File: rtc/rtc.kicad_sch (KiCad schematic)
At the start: 9 parts, among them J1 Conn_01x04_Pin, U1 PCF8563T/5_518, Y1 Crystal

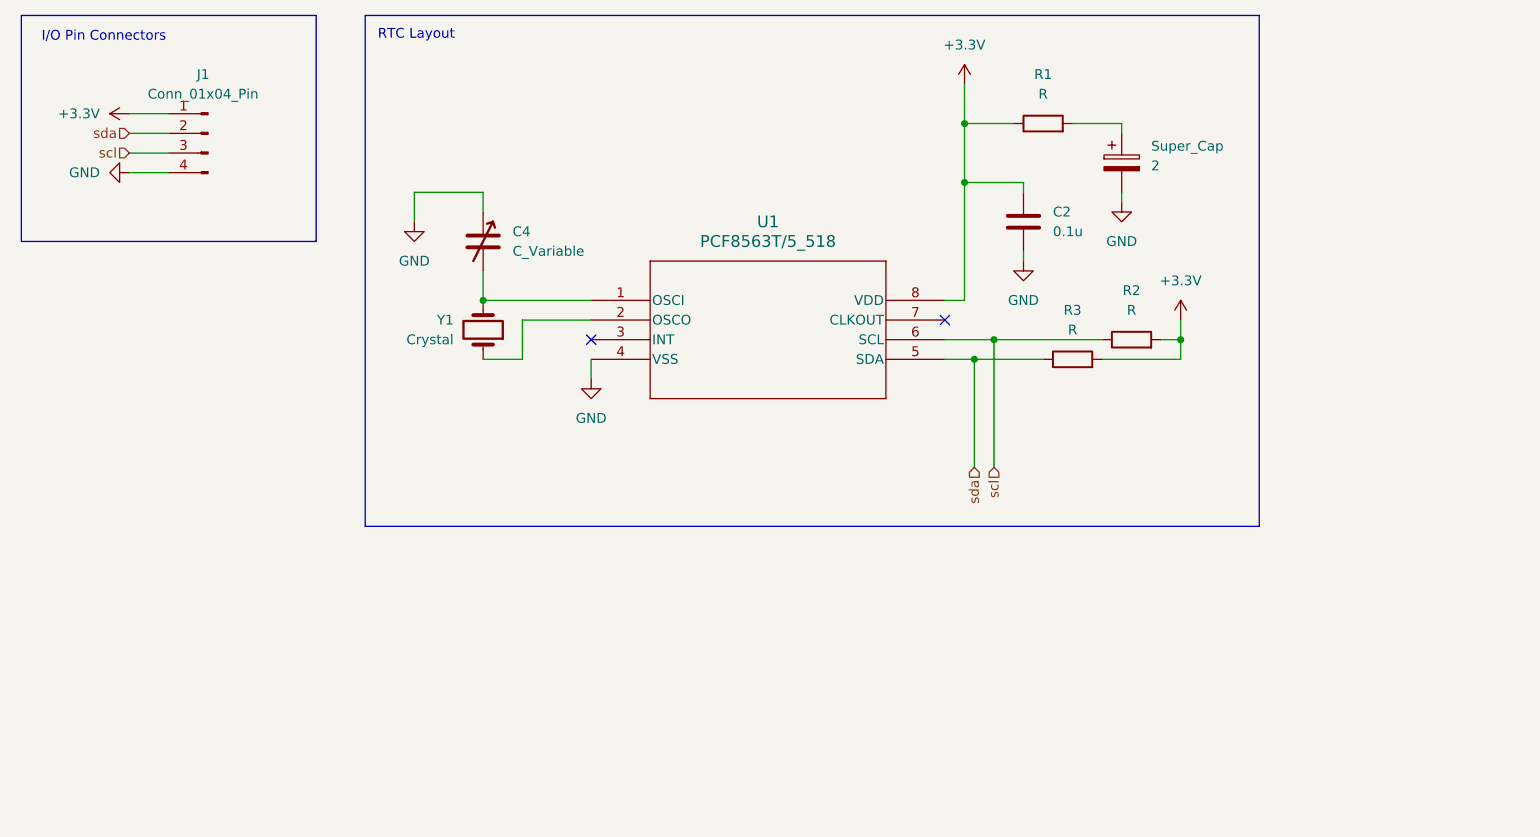
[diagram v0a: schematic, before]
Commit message: rtc schematic progress
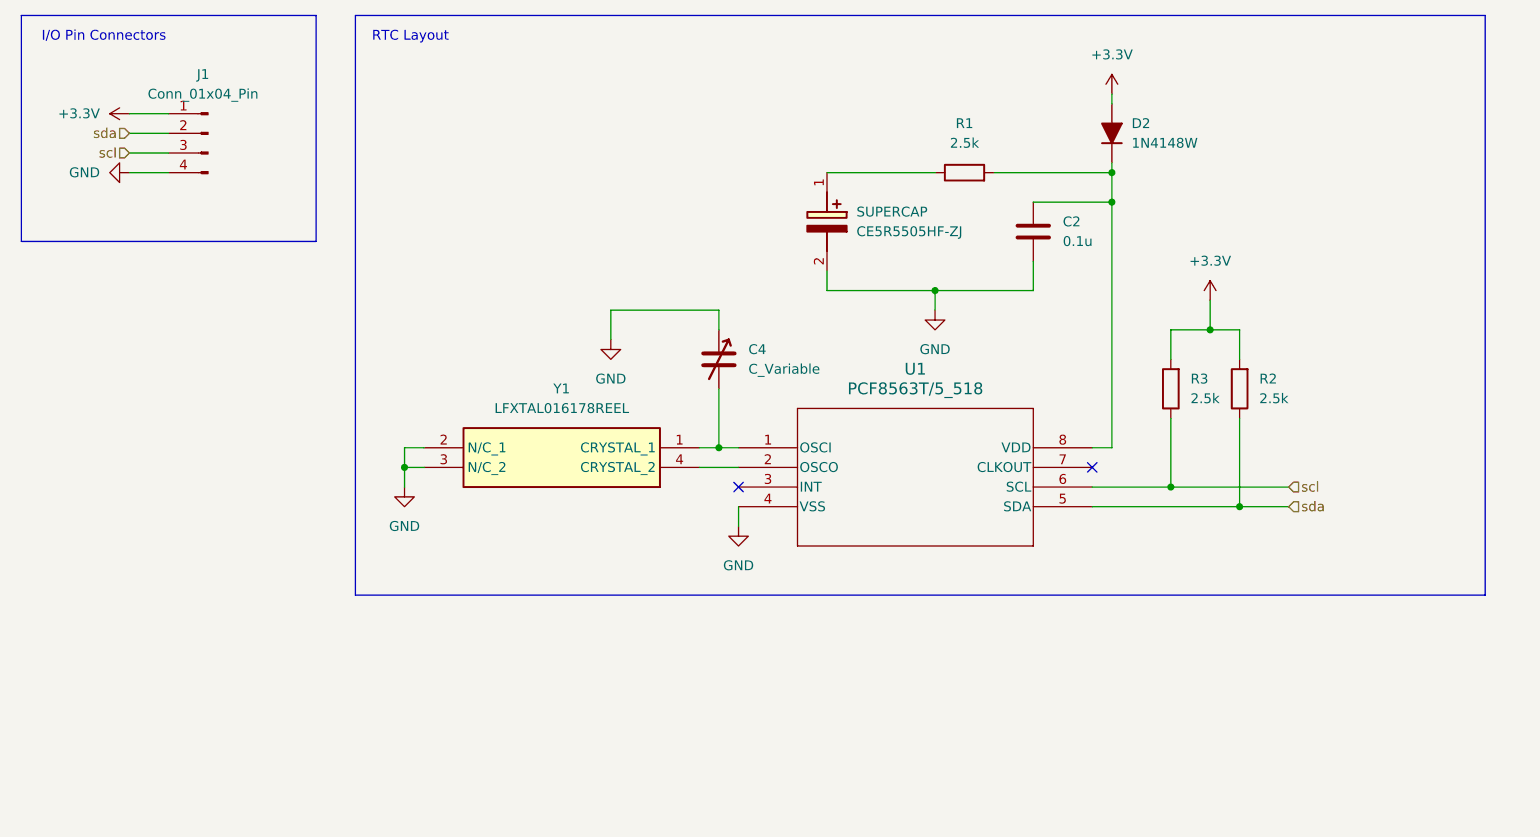
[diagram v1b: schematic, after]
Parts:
- removed Super_Cap: 2, symbol Device:C_Polarized
- removed Y1: Crystal, symbol Device:Crystal
- added D2: 1N4148W, PCM_Diode_SMD_AKL:D_SOD-123, symbol PCM_Diode_AKL:1N4148W
- added SUPERCAP: CE5R5505HF-ZJ, CE5R5505HFZJ, symbol CE5R5505HF-ZJ:CE5R5505HF-ZJ
- added Y1: LFXTAL016178REEL, LFXTAL016178REEL, symbol LFXTAL016178REEL:LFXTAL016178REEL
- R1, R2, R3: value R -> 2.5k
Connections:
- net +3.3V: now also D2.2 (A); no longer C2.1, R1.1, U1.8 (VDD)
- net GND: now also SUPERCAP.2 (-), Y1.2 (N/C_1), Y1.3 (N/C_2)
- net scl: now also R3.1; no longer R2.1
- net sda: now also R2.1; no longer R3.1
- net at C4.2, U1.1 (OSCI): now also Y1.1 (CRYSTAL_1)
- net at U1.2 (OSCO): now also Y1.4 (CRYSTAL_2)
- net at R1.2: now also C2.1, U1.8 (VDD), D2.1 (K)
- new net: R1.1, SUPERCAP.1 (+)
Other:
- moved on the sheet: C2, C4, R1, R2, R3, U1

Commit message: finished rtc schematic
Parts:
- removed C4: C_Variable, symbol Device:C_Variable
- added C1: C, Capacitor_SMD:C_0402_1005Metric_Pad0.74x0.62mm_HandSolder, symbol Device:C
- C2: footprint (none) -> Capacitor_SMD:C_0402_1005Metric_Pad0.74x0.62mm_HandSolder
- J1: footprint (none) -> Connector_PinHeader_2.54mm:PinHeader_1x04_P2.54mm_Horizontal
- R1: value 2.5k -> 20k; footprint (none) -> Resistor_SMD:R_0402_1005Metric_Pad0.72x0.64mm_HandSolder
- R2, R3: footprint (none) -> Resistor_SMD:R_0402_1005Metric_Pad0.72x0.64mm_HandSolder
- SUPERCAP1: renamed from SUPERCAP; value CE5R5505HF-ZJ -> 5; footprint CE5R5505HFZJ -> pcb_footprints:CE5R5505HFZJ
- U1: footprint U_SO8_NXP -> pcb_footprints:PCF8563T_5_518_U_SO8_NXP
- Y1: footprint LFXTAL016178REEL -> pcb_footprints:LFXTAL016178REEL
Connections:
- net GND: now also C1.1
- net at U1.1 (OSCI), Y1.1 (CRYSTAL_1): now also C1.2
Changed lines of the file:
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@@
 			)
 		)
-		(property "Footprint" "U_SO8_NXP"
+		(property "Footprint" "pcb_footprints:PCF8563T_5_518_U_SO8_NXP"
 			(at 125.73 86.36 0)
 			(effects
@@
 			)
 		)
-		(property "Footprint" "LFXTAL016178REEL"
+		(property "Footprint" "pcb_footprints:LFXTAL016178REEL"
 			(at 88.9 -6.02 0)
 			(effects
@@
 			)
 		)
-		(property "Footprint" ""
+		(property "Footprint" "Connector_PinHeader_2.54mm:PinHeader_1x04_P2.54mm_Horizontal"
 			(at 57.15 45.72 0)
 			(effects
@@
 			)
 		)
-		(property "Value" "2.5k"
+		(property "Value" "20k"
 			(at 154.94 46.99 90)
 			(effects
@@
 			)
 		)
-		(property "Footprint" ""
+		(property "Footprint" "Resistor_SMD:R_0402_1005Metric_Pad0.72x0.64mm_HandSolder"
 			(at 154.94 52.578 90)
 			(effects
@@
 			)
 		)
-		(property "Footprint" ""
+		(property "Footprint" "Capacitor_SMD:C_0402_1005Metric_Pad0.74x0.62mm_HandSolder"
 			(at 164.7952 62.23 0)
 			(effects
@@
 			)
 		)
-		(property "Footprint" ""
+		(property "Footprint" "Resistor_SMD:R_0402_1005Metric_Pad0.72x0.64mm_HandSolder"
 			(at 183.388 78.74 90)
 			(effects
@@
 		(dnp no)
 		(fields_autoplaced yes)
-		(property "Reference" "SUPERCAP"
+		(property "Reference" "SUPERCAP1"
 			(at 140.97 55.8799 90)
 			(effects
@@
 			)
 		)
-		(property "Value" "CE5R5505HF-ZJ"
+		(property "Value" "5"
 			(at 140.97 58.4199 90)
 			(effects
@@
 			)
 		)
-		(property "Footprint" "CE5R5505HFZJ"
+		(property "Footprint" "pcb_footprints:CE5R5505HFZJ"
 			(at 40.97 59.69 0)
 			(effects
@@
 			(project ""
 				(path "/818bb878-dad3-4efb-a0ef-59b01bf8b5c9"
-					(reference "SUPERCAP")
+					(reference "SUPERCAP1")
 					(unit 1)
 				)
@@
 			)
 		)
-		(property "Footprint" ""
+		(property "Footprint" "Resistor_SMD:R_0402_1005Metric_Pad0.72x0.64mm_HandSolder"
 			(at 192.278 78.74 90)
 			(effects
@@
 	)
 	(symbol
-		(lib_id "Device:C_Variable")
+		(lib_id "Device:C")
 		(at 123.19 74.93 0)
 		(unit 1)
@@
 		(dnp no)
 		(fields_autoplaced yes)
-		(property "Reference" "C4"
+		(property "Reference" "C1"
 			(at 127 73.6599 0)
 			(effects
@@
 			)
 		)
-		(property "Value" "C_Variable"
+		(property "Value" "C"
 			(at 127 76.1999 0)
 			(effects
@@
 			)
 		)
-		(property "Footprint" ""
-			(at 123.19 74.93 0)
+		(property "Footprint" "Capacitor_SMD:C_0402_1005Metric_Pad0.74x0.62mm_HandSolder"
+			(at 124.1552 78.74 0)
 			(effects
 				(font
@@
 			)
 		)
-		(property "Description" "Variable capacitor"
+		(property "Description" "Unpolarized capacitor"
 			(at 123.19 74.93 0)
 			(effects
@@
 			(project ""
 				(path "/818bb878-dad3-4efb-a0ef-59b01bf8b5c9"
-					(reference "C4")
-					(unit 1)
-				)
+					(reference "C1")
+					(unit 1)
+				)

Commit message: finished rtc schematic
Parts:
- removed D2: 1N4148W, PCM_Diode_SMD_AKL:D_SOD-123, symbol PCM_Diode_AKL:1N4148W
- removed J1: Conn_01x04_Pin, Connector_PinHeader_2.54mm:PinHeader_1x04_P2.54mm_Horizontal, symbol Connector:Conn_01x04_Pin
- added C3: C, Capacitor_SMD:C_0402_1005Metric_Pad0.74x0.62mm_HandSolder, symbol Device:C
- added D2: RB751V-40X_R1, pcb_footprints:SODFL2512X90N, symbol PCM_Diode_Schottky_AKL:D_Schottky_Generic
- added J1: Conn_02x03_Counter_Clockwise, Connector_PinHeader_2.54mm:PinHeader_2x03_P2.54mm_Vertical, symbol Connector_Generic:Conn_02x03_Counter_Clockwise
- added J2, J3, J4: Conn_01x04, pcb_footprints:JST_SH_BM04B-SRSS-TB_1x04-1MP_P1.00mm_Vertical, symbol Connector_Generic:Conn_01x04
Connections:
- net +3.3V: now also D2.2 (A), J1.1 (Pin_1), J2.2 (Pin_2), J3.2 (Pin_2), J4.2 (Pin_2)
- net GND: now also C1.2, C3.2, J1.4 (Pin_4), J2.1 (Pin_1), J3.1 (Pin_1), J4.1 (Pin_1); no longer C1.1
- net scl: now also J1.3 (Pin_3), J2.4 (Pin_4), J3.4 (Pin_4), J4.4 (Pin_4)
- net sda: now also J1.2 (Pin_2), J2.3 (Pin_3), J3.3 (Pin_3), J4.3 (Pin_3)
- net at U1.1 (OSCI), Y1.1 (CRYSTAL_1): now also C1.1; no longer C1.2
- net at U1.2 (OSCO), Y1.4 (CRYSTAL_2): now also C3.1
- net at C2.1, R1.2, U1.8 (VDD): now also D2.1 (K)
- no-connect marks 2 -> 4
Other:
- note added: "JST Connectors"
- moved on the sheet: C1, C2, R1, R2, R3, SUPERCAP1, U1, Y1

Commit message: finished rtc pcb
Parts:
- removed J1: Conn_02x03_Counter_Clockwise, Connector_PinHeader_2.54mm:PinHeader_2x03_P2.54mm_Vertical, symbol Connector_Generic:Conn_02x03_Counter_Clockwise
- added J1: Conn_02x03_Odd_Even, Connector_PinHeader_2.54mm:PinHeader_2x03_P2.54mm_Vertical, symbol Connector_Generic:Conn_02x03_Odd_Even
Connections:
- net +3.3V: now also J1.1 (Pin_1)
- net GND: now also J1.6 (Pin_6)
- net scl: now also J1.5 (Pin_5)
- net sda: now also J1.3 (Pin_3)
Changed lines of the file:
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@@
 	)
 	(no_connect
-		(at 180.34 87.63)
+		(at 60.96 46.99)
 	)
 	(no_connect
-		(at 60.96 46.99)
+		(at 180.34 87.63)
 	)
 	(no_connect
@@
 	(wire
 		(pts
-			(xy 43.18 46.99) (xy 48.26 46.99)
-		)
-		(stroke
-			(width 0)
-			(type default)
-		)
-	)
-	(wire
-		(pts
 			(xy 44.45 111.76) (xy 49.53 111.76)
 		)
@@
 	(wire
 		(pts
-			(xy 172.72 53.34) (xy 182.88 53.34)
+			(xy 43.18 49.53) (xy 48.26 49.53)
 		)
 		(stroke
@@
 	(wire
 		(pts
-			(xy 43.18 44.45) (xy 48.26 44.45)
+			(xy 172.72 53.34) (xy 182.88 53.34)
 		)
 		(stroke
@@
 	(wire
 		(pts
-			(xy 113.03 80.01) (xy 115.57 80.01)
+			(xy 43.18 44.45) (xy 48.26 44.45)
 		)
 		(stroke
@@
 	(wire
 		(pts
-			(xy 43.18 49.53) (xy 48.26 49.53)
+			(xy 113.03 80.01) (xy 115.57 80.01)
 		)
 		(stroke
@@
 		)
 	)
+	(wire
+		(pts
+			(xy 43.18 46.99) (xy 48.26 46.99)
+		)
+		(stroke
+			(width 0)
+			(type default)
+		)
+	)
 	(image
 		(at 52.07 66.04)
@@
 		)
 	)
-	(hierarchical_label "scl"
+	(global_label "scl"
 		(shape input)
-		(at 205.74 90.17 0)
+		(at 43.18 49.53 180)
+		(fields_autoplaced yes)
 		(effects
 			(font
 				(size 1.27 1.27)
 			)
-			(justify left)
+			(justify right)
+		)
+		(property "Intersheetrefs" "${INTERSHEET_REFS}"
+			(at 37.4129 49.53 0)
+			(effects
+				(font
+					(size 1.27 1.27)
+				)
+				(justify right)
+				(hide yes)
+			)
 		)
 	)
-	(hierarchical_label "sda"
+	(global_label "sda"
 		(shape input)
-		(at 44.45 111.76 180)
+		(at 205.74 92.71 0)
+		(fields_autoplaced yes)
 		(effects
 			(font
 				(size 1.27 1.27)
 			)
-			(justify right)
+			(justify left)
+		)
+		(property "Intersheetrefs" "${INTERSHEET_REFS}"
+			(at 212.0513 92.71 0)
+			(effects
+				(font
+					(size 1.27 1.27)
+				)
+				(justify left)
+				(hide yes)
+			)
 		)
 	)
-	(hierarchical_label "sda"
+	(global_label "sda"
 		(shape input)
-		(at 43.18 46.99 180)
+		(at 44.45 125.73 180)
+		(fields_autoplaced yes)
 		(effects
 			(font
@@
 			(justify right)
 		)
+		(property "Intersheetrefs" "${INTERSHEET_REFS}"
+			(at 38.1387 125.73 0)
+			(effects
+				(font
+					(size 1.27 1.27)
+				)
+				(justify right)
+				(hide yes)
+			)
+		)
 	)
-	(hierarchical_label "scl"
+	(global_label "sda"
 		(shape input)
-		(at 43.18 49.53 180)
+		(at 44.45 97.79 180)
+		(fields_autoplaced yes)
 		(effects
 			(font
@@
 			(justify right)
 		)
+		(property "Intersheetrefs" "${INTERSHEET_REFS}"
+			(at 38.1387 97.79 0)
+			(effects
+				(font
+					(size 1.27 1.27)
+				)
+				(justify right)
+				(hide yes)
+			)
+		)
 	)
-	(hierarchical_label "sda"
+	(global_label "sda"
 		(shape input)
-		(at 205.74 92.71 0)
+		(at 44.45 111.76 180)
+		(fields_autoplaced yes)
 		(effects
 			(font
 				(size 1.27 1.27)
 			)
-			(justify left)
+			(justify right)
+		)
+		(property "Intersheetrefs" "${INTERSHEET_REFS}"
+			(at 38.1387 111.76 0)
+			(effects
+				(font
+					(size 1.27 1.27)
+				)
+				(justify right)
+				(hide yes)
+			)
 		)
 	)
-	(hierarchical_label "sda"
+	(global_label "scl"
 		(shape input)
-		(at 44.45 125.73 180)
+		(at 44.45 100.33 180)
+		(fields_autoplaced yes)
 		(effects
 			(font
@@
 			(justify right)
 		)
+		(property "Intersheetrefs" "${INTERSHEET_REFS}"
+			(at 38.6829 100.33 0)
+			(effects
+				(font
+					(size 1.27 1.27)
+				)
+				(justify right)
+				(hide yes)
+			)
+		)
 	)
-	(hierarchical_label "scl"
+	(global_label "scl"
 		(shape input)
-		(at 44.45 100.33 180)
+		(at 205.74 90.17 0)
+		(fields_autoplaced yes)
 		(effects
 			(font
 				(size 1.27 1.27)
 			)
-			(justify right)
+			(justify left)
+		)
+		(property "Intersheetrefs" "${INTERSHEET_REFS}"
+			(at 211.5071 90.17 0)
+			(effects
+				(font
+					(size 1.27 1.27)
+				)
+				(justify left)
+				(hide yes)
+			)
 		)
 	)
-	(hierarchical_label "scl"
+	(global_label "scl"
 		(shape input)
-		(at 44.45 114.3 180)
+		(at 44.45 128.27 180)
+		(fields_autoplaced yes)
 		(effects
 			(font
@@
 			(justify right)
 		)
+		(property "Intersheetrefs" "${INTERSHEET_REFS}"
+			(at 38.6829 128.27 0)
+			(effects
+				(font
+					(size 1.27 1.27)
+				)
+				(justify right)
+				(hide yes)
+			)
+		)
 	)
-	(hierarchical_label "scl"
+	(global_label "scl"
 		(shape input)
-		(at 44.45 128.27 180)
+		(at 44.45 114.3 180)
+		(fields_autoplaced yes)
 		(effects
 			(font
@@
 			(justify right)
 		)
+		(property "Intersheetrefs" "${INTERSHEET_REFS}"
+			(at 38.6829 114.3 0)
+			(effects
+				(font
+					(size 1.27 1.27)
+				)
+				(justify right)
+				(hide yes)
+			)
+		)
 	)
-	(hierarchical_label "sda"
+	(global_label "sda"
 		(shape input)
-		(at 44.45 97.79 180)
+		(at 43.18 46.99 180)
+		(fields_autoplaced yes)
 		(effects
 			(font
@@
 			(justify right)
 		)
+		(property "Intersheetrefs" "${INTERSHEET_REFS}"
+			(at 36.8687 46.99 0)
+			(effects
+				(font
+					(size 1.27 1.27)
+				)
+				(justify right)
+				(hide yes)
+			)
+		)
 	)
 	(symbol
@@
 	)
 	(symbol
+		(lib_id "Connector_Generic:Conn_02x03_Odd_Even")
+		(at 53.34 46.99 0)
+		(unit 1)
+		(exclude_from_sim no)
+		(in_bom yes)
+		(on_board yes)
+		(dnp no)
+		(fields_autoplaced yes)
+		(property "Reference" "J1"
+			(at 54.61 38.1 0)
+			(effects
+				(font
+					(size 1.27 1.27)
+				)
+			)
+		)
+		(property "Value" "Conn_02x03_Odd_Even"
+			(at 54.61 40.64 0)
+			(effects
+				(font
+					(size 1.27 1.27)
+				)
+			)
+		)
+		(property "Footprint" "Connector_PinHeader_2.54mm:PinHeader_2x03_P2.54mm_Vertical"
+			(at 53.34 46.99 0)
+			(effects
+				(font
+					(size 1.27 1.27)
+				)
+				(hide yes)
+			)
+		)
+		(property "Datasheet" "~"
+			(at 53.34 46.99 0)
+			(effects
+				(font
+					(size 1.27 1.27)
+				)
+				(hide yes)
+			)
+		)
+		(property "Description" "Generic connector, double row, 02x03, odd/even pin numbering scheme (row 1 odd numbers, row 2 even numbers), script generated (kicad-library-utils/schlib/autogen/connector/)"
+			(at 53.34 46.99 0)
+			(effects
+				(font
+					(size 1.27 1.27)
+				)
+				(hide yes)
+			)
+		)
+		(pin "3"
+		)
+		(pin "1"
+		)
+		(pin "4"
+		)
+		(pin "6"
+		)
+		(pin "2"
+		)
+		(pin "5"
+		)
+		(instances
+			(project ""
+				(path "/818bb878-dad3-4efb-a0ef-59b01bf8b5c9"
+					(reference "J1")
+					(unit 1)
+				)
+			)
+		)
+	)
+	(symbol
 		(lib_id "PCM_Diode_Schottky_AKL:D_Schottky_Generic")
 		(at 182.88 44.45 270)
@@
 					(unit 1)
 				)
-			)
-		)
-	)
-	(symbol
-		(lib_id "Connector_Generic:Conn_02x03_Counter_Clockwise")
-		(at 53.34 46.99 0)
-		(unit 1)
-		(exclude_from_sim no)
-		(in_bom yes)
-		(on_board yes)
-		(dnp no)
-		(fields_autoplaced yes)
-		(property "Reference" "J1"
-			(at 54.61 38.1 0)
-			(effects
-				(font
-					(size 1.27 1.27)
-				)
-			)
-		)
-		(property "Value" "Conn_02x03_Counter_Clockwise"
-			(at 54.61 40.64 0)
-			(effects
-				(font
-					(size 1.27 1.27)
-				)
-			)
-		)
-		(property "Footprint" "Connector_PinHeader_2.54mm:PinHeader_2x03_P2.54mm_Vertical"
-			(at 53.34 46.99 0)
-			(effects
-				(font
-					(size 1.27 1.27)
-				)
-				(hide yes)
-			)
-		)
-		(property "Datasheet" "~"
-			(at 53.34 46.99 0)
-			(effects
-				(font
-					(size 1.27 1.27)
-				)
-				(hide yes)
-			)
-		)
-		(property "Description" "Generic connector, double row, 02x03, counter clockwise pin numbering scheme (similar to DIP package numbering), script generated (kicad-library-utils/schlib/autogen/connector/)"
-			(at 53.34 46.99 0)
-			(effects
-				(font
-					(size 1.27 1.27)
-				)
-				(hide yes)
-			)
-		)
-		(pin "6"
-		)
-		(pin "1"
-		)
-		(pin "4"
-		)
-		(pin "3"
-		)
-		(pin "5"
-		)
-		(pin "2"
-		)
-		(instances
-			(project ""
-				(path "/818bb878-dad3-4efb-a0ef-59b01bf8b5c9"
-					(reference "J1")
-					(unit 1)
-				)

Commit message: rtc pcb iteration 2
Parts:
- C1, C3: value C -> 24p
- J1: footprint Connector_PinHeader_2.54mm:PinHeader_2x03_P2.54mm_Vertical -> Connector_PinSocket_2.54mm:PinSocket_2x03_P2.54mm_Vertical
- J2, J3, J4: footprint pcb_footprints:JST_SH_BM04B-SRSS-TB_1x04-1MP_P1.00mm_Vertical -> pcb_footprints:SM04BSRSSTB
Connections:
- net +3.3V: now also J1.6 (Pin_6); no longer J1.1 (Pin_1)
- net GND: now also J1.1 (Pin_1); no longer J1.6 (Pin_6)
- net scl: now also J1.2 (Pin_2); no longer J1.5 (Pin_5)
- net sda: now also J1.4 (Pin_4); no longer J1.3 (Pin_3)
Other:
- moved on the sheet: J1
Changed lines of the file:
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@@
 	(wire
 		(pts
-			(xy 43.18 44.45) (xy 48.26 44.45)
+			(xy 113.03 80.01) (xy 115.57 80.01)
 		)
 		(stroke
@@
 	(wire
 		(pts
-			(xy 113.03 80.01) (xy 115.57 80.01)
+			(xy 199.39 81.28) (xy 199.39 92.71)
 		)
 		(stroke
@@
 	(wire
 		(pts
-			(xy 199.39 81.28) (xy 199.39 92.71)
+			(xy 172.72 60.96) (xy 172.72 64.77)
 		)
 		(stroke
@@
 	(wire
 		(pts
-			(xy 172.72 60.96) (xy 172.72 64.77)
+			(xy 43.18 44.45) (xy 48.26 44.45)
 		)
 		(stroke
@@
 	(wire
 		(pts
+			(xy 43.18 46.99) (xy 48.26 46.99)
+		)
+		(stroke
+			(width 0)
+			(type default)
+		)
+	)
+	(wire
+		(pts
 			(xy 113.03 100.33) (xy 123.19 100.33)
 		)
@@
 	(wire
 		(pts
+			(xy 60.96 49.53) (xy 63.5 49.53)
+		)
+		(stroke
+			(width 0)
+			(type default)
+		)
+	)
+	(wire
+		(pts
 			(xy 113.03 100.33) (xy 113.03 97.79)
 		)
@@
 	(wire
 		(pts
-			(xy 60.96 49.53) (xy 63.5 49.53)
-		)
-		(stroke
-			(width 0)
-			(type default)
-		)
-	)
-	(wire
-		(pts
 			(xy 182.88 48.26) (xy 182.88 49.53)
 		)
@@
 		)
 	)
-	(wire
-		(pts
-			(xy 43.18 46.99) (xy 48.26 46.99)
-		)
-		(stroke
-			(width 0)
-			(type default)
-		)
-	)
 	(image
 		(at 52.07 66.04)
@@
 		(on_board yes)
 		(dnp no)
-		(fields_autoplaced yes)
 		(property "Reference" "#PWR02"
 			(at 63.5 57.15 0)
@@
 	(symbol
 		(lib_id "Connector_Generic:Conn_02x03_Odd_Even")
-		(at 53.34 46.99 0)
+		(at 55.88 46.99 180)
 		(unit 1)
 		(exclude_from_sim no)
@@
 		(on_board yes)
 		(dnp no)
-		(fields_autoplaced yes)
 		(property "Reference" "J1"
-			(at 54.61 38.1 0)
+			(at 54.61 41.656 0)
 			(effects
 				(font
@@
 		)
 		(property "Value" "Conn_02x03_Odd_Even"
-			(at 54.61 40.64 0)
+			(at 54.61 39.116 0)
 			(effects
 				(font
@@
 			)
 		)
-		(property "Footprint" "Connector_PinHeader_2.54mm:PinHeader_2x03_P2.54mm_Vertical"
-			(at 53.34 46.99 0)
+		(property "Footprint" "Connector_PinSocket_2.54mm:PinSocket_2x03_P2.54mm_Vertical"
+			(at 55.88 46.99 0)
 			(effects
 				(font
@@
 		)
 		(property "Datasheet" "~"
-			(at 53.34 46.99 0)
+			(at 55.88 46.99 0)
 			(effects
 				(font
@@
 		)
 		(property "Description" "Generic connector, double row, 02x03, odd/even pin numbering scheme (row 1 odd numbers, row 2 even numbers), script generated (kicad-library-utils/schlib/autogen/connector/)"
-			(at 53.34 46.99 0)
+			(at 55.88 46.99 0)
 			(effects
 				(font
@@
 			)
 		)
-		(property "Footprint" "pcb_footprints:JST_SH_BM04B-SRSS-TB_1x04-1MP_P1.00mm_Vertical"
+		(property "Footprint" "pcb_footprints:SM04BSRSSTB"
 			(at 54.61 109.22 0)
 			(effects
@@
 			)
 		)
-		(property "Footprint" "pcb_footprints:JST_SH_BM04B-SRSS-TB_1x04-1MP_P1.00mm_Vertical"
+		(property "Footprint" "pcb_footprints:SM04BSRSSTB"
 			(at 54.61 123.19 0)
 			(effects
@@
 			)
 		)
-		(property "Value" "C"
+		(property "Value" "24p"
 			(at 116.84 95.2499 0)
 			(effects
@@
 			)
 		)
-		(property "Value" "C"
+		(property "Value" "24p"
 			(at 127 95.2499 0)
 			(effects
@@
 			)
 		)
-		(property "Footprint" "pcb_footprints:JST_SH_BM04B-SRSS-TB_1x04-1MP_P1.00mm_Vertical"
+		(property "Footprint" "pcb_footprints:SM04BSRSSTB"
 			(at 54.61 95.25 0)
 			(effects
